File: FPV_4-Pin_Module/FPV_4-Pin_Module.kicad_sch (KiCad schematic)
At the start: 2 parts, among them J1 Conn_01x10_Socket, J2 Conn_01x10_Socket

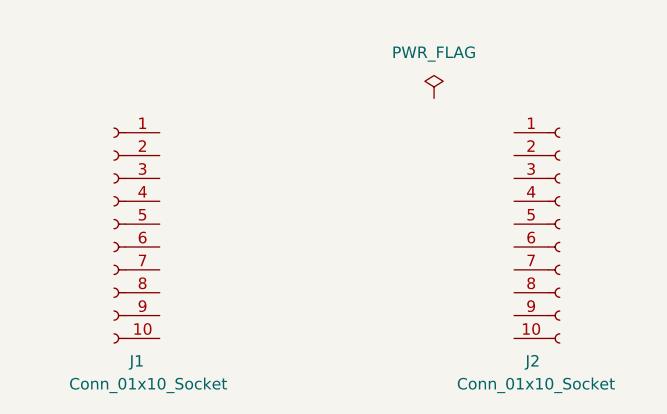
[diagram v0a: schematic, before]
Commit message: Adding FPV 4-pin interface module
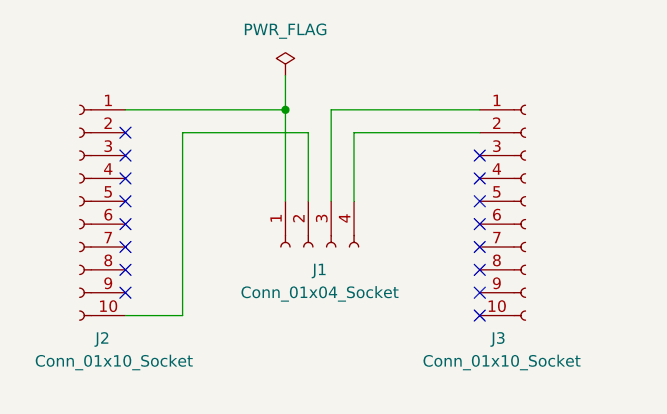
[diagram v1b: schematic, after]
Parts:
- removed J1: Conn_01x10_Socket, Connector_PinSocket_2.00mm:PinSocket_1x10_P2.00mm_Vertical, symbol Connector:Conn_01x10_Socket
- added J1: Conn_01x04_Socket, Connector_JST:JST_PH_B4B-PH-K_1x04_P2.00mm_Vertical, symbol Connector:Conn_01x04_Socket
- added J3: Conn_01x10_Socket, Connector_PinSocket_2.00mm:PinSocket_1x10_P2.00mm_Vertical, symbol Connector:Conn_01x10_Socket
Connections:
- net at J2.1 (Pin_1): now also J1.1 (Pin_1)
- net at J2.10 (Pin_10): now also J1.2 (Pin_2)
- new net: J1.3 (Pin_3), J3.1 (Pin_1)
- new net: J1.4 (Pin_4), J3.2 (Pin_2)
- no-connect marks 0 -> 16
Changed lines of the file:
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@@
 (kicad_sch (version 20230121) (generator eeschema)
   (paper "A4")
-  (symbol (lib_id "Connector:Conn_01x10_Socket") (at 121.92 95.25 0) (mirror y) (unit 1)
+  (junction (at 140.97 82.55) (diameter 0) (color 0 0 0 0)
+  )
+  (no_connect (at 123.19 100.33))
+  (no_connect (at 123.19 95.25))
+  (no_connect (at 162.56 100.33))
+  (no_connect (at 162.56 102.87))
+  (no_connect (at 123.19 90.17))
+  (no_connect (at 123.19 92.71))
+  (no_connect (at 162.56 97.79))
+  (no_connect (at 123.19 85.09))
+  (no_connect (at 162.56 87.63))
+  (no_connect (at 123.19 87.63))
+  (no_connect (at 162.56 105.41))
+  (no_connect (at 162.56 95.25))
+  (no_connect (at 123.19 102.87))
+  (no_connect (at 123.19 97.79))
+  (no_connect (at 162.56 92.71))
+  (no_connect (at 162.56 90.17))
+  (wire (pts (xy 129.54 105.41) (xy 123.19 105.41))
+    (stroke (width 0) (type default))
+  )
+  (wire (pts (xy 140.97 92.71) (xy 140.97 82.55))
+    (stroke (width 0) (type default))
+  )
+  (wire (pts (xy 146.05 82.55) (xy 162.56 82.55))
+    (stroke (width 0) (type default))
+  )
+  (wire (pts (xy 148.59 92.71) (xy 148.59 85.09))
+    (stroke (width 0) (type default))
+  )
+  (wire (pts (xy 143.51 92.71) (xy 143.51 85.09))
+    (stroke (width 0) (type default))
+  )
+  (wire (pts (xy 143.51 85.09) (xy 129.54 85.09))
+    (stroke (width 0) (type default))
+  )
+  (wire (pts (xy 146.05 92.71) (xy 146.05 82.55))
+    (stroke (width 0) (type default))
+  )
+  (wire (pts (xy 129.54 85.09) (xy 129.54 105.41))
+    (stroke (width 0) (type default))
+  )
+  (wire (pts (xy 140.97 78.74) (xy 140.97 82.55))
+    (stroke (width 0) (type default))
+  )
+  (wire (pts (xy 140.97 82.55) (xy 123.19 82.55))
+    (stroke (width 0) (type default))
+  )
+  (wire (pts (xy 148.59 85.09) (xy 162.56 85.09))
+    (stroke (width 0) (type default))
+  )
+  (symbol (lib_id "Connector:Conn_01x10_Socket") (at 167.64 92.71 0) (unit 1)
     (in_bom yes) (on_board yes) (dnp no)
-    (property "Reference" "J1" (at 124.46 110.49 0)
-      (effects (font (size 1.27 1.27)))
+    (property "Reference" "J3" (at 163.83 107.95 0)
+      (effects (font (size 1.27 1.27)) (justify left))
     )
-    (property "Value" "Conn_01x10_Socket" (at 125.73 113.03 0)
-      (effects (font (size 1.27 1.27)))
+    (property "Value" "Conn_01x10_Socket" (at 156.21 110.49 0)
+      (effects (font (size 1.27 1.27)) (justify left))
     )
-    (property "Footprint" "Connector_PinSocket_2.00mm:PinSocket_1x10_P2.00mm_Vertical" (at 121.92 95.25 0)
+    (property "Footprint" "Connector_PinSocket_2.00mm:PinSocket_1x10_P2.00mm_Vertical" (at 167.64 92.71 0)
       (effects (font (size 1.27 1.27)) hide)
     )
-    (property "Datasheet" "~" (at 121.92 95.25 0)
+    (property "Datasheet" "~" (at 167.64 92.71 0)
       (effects (font (size 1.27 1.27)) hide)
     )
@@
       (project "FPV_4-Pin_Module"
         (path "/7bf13dc3-6a85-4b7a-9483-4a4f8f99eecc"
-          (reference "J1") (unit 1)
+          (reference "J3") (unit 1)
         )
       )
       (project "USB_Module"
         (path "/d452682e-4b72-4fc8-ac9a-c22d1abda260"
-          (reference "J2") (unit 1)
+          (reference "J3") (unit 1)
         )
       )
       (project "FPV_3-Pin_Module"
         (path "/d88b4443-d914-4b47-8a50-2a5201342e50"
+          (reference "J3") (unit 1)
+        )
+      )
+    )
+  )
+  (symbol (lib_id "Connector:Conn_01x04_Socket") (at 143.51 97.79 90) (mirror x) (unit 1)
+    (in_bom yes) (on_board yes) (dnp no)
+    (property "Reference" "J1" (at 144.78 100.33 90)
+      (effects (font (size 1.27 1.27)))
+    )
+    (property "Value" "Conn_01x04_Socket" (at 144.78 102.87 90)
+      (effects (font (size 1.27 1.27)))
+    )
+    (property "Footprint" "Connector_JST:JST_PH_B4B-PH-K_1x04_P2.00mm_Vertical" (at 143.51 97.79 0)
+      (effects (font (size 1.27 1.27)) hide)
+    )
+    (property "Datasheet" "~" (at 143.51 97.79 0)
+      (effects (font (size 1.27 1.27)) hide)
+    )
+    (pin "1")
+    (pin "2")
+    (pin "3")
+    (pin "4")
+    (instances
+      (project "FPV_4-Pin_Module"
+        (path "/7bf13dc3-6a85-4b7a-9483-4a4f8f99eecc"
           (reference "J1") (unit 1)
         )
@@
     )
   )
-  (symbol (lib_id "power:PWR_FLAG") (at 157.48 81.28 0) (unit 1)
-    (in_bom yes) (on_board yes) (dnp no) (fields_autoplaced)
-    (property "Reference" "#FLG01" (at 157.48 79.375 0)
+  (symbol (lib_id "Connector:Conn_01x10_Socket") (at 118.11 92.71 0) (mirror y) (unit 1)
+    (in_bom yes) (on_board yes) (dnp no)
+    (property "Reference" "J2" (at 120.65 107.95 0)
+      (effects (font (size 1.27 1.27)))
+    )
+    (property "Value" "Conn_01x10_Socket" (at 121.92 110.49 0)
+      (effects (font (size 1.27 1.27)))
+    )
+    (property "Footprint" "Connector_PinSocket_2.00mm:PinSocket_1x10_P2.00mm_Vertical" (at 118.11 92.71 0)
       (effects (font (size 1.27 1.27)) hide)
     )
-    (property "Value" "PWR_FLAG" (at 157.48 76.2 0)
-      (effects (font (size 1.27 1.27)))
-    )
-    (property "Footprint" "" (at 157.48 81.28 0)
-      (effects (font (size 1.27 1.27)) hide)
-    )
-    (property "Datasheet" "~" (at 157.48 81.28 0)
-      (effects (font (size 1.27 1.27)) hide)
-    )
-    (pin "1")
-    (instances
-      (project "FPV_4-Pin_Module"
-        (path "/7bf13dc3-6a85-4b7a-9483-4a4f8f99eecc"
-          (reference "#FLG01") (unit 1)
-        )
-      )
-      (project "USB_Module"
-        (path "/d452682e-4b72-4fc8-ac9a-c22d1abda260"
-          (reference "#FLG02") (unit 1)
-        )
-      )
-      (project "FPV_3-Pin_Module"
-        (path "/d88b4443-d914-4b47-8a50-2a5201342e50"
-          (reference "#FLG02") (unit 1)
-        )
-      )
-    )
-  )
-  (symbol (lib_id "Connector:Conn_01x10_Socket") (at 171.45 95.25 0) (unit 1)
-    (in_bom yes) (on_board yes) (dnp no)
-    (property "Reference" "J2" (at 167.64 110.49 0)
-      (effects (font (size 1.27 1.27)) (justify left))
-    )
-    (property "Value" "Conn_01x10_Socket" (at 160.02 113.03 0)
-      (effects (font (size 1.27 1.27)) (justify left))
-    )
-    (property "Footprint" "Connector_PinSocket_2.00mm:PinSocket_1x10_P2.00mm_Vertical" (at 171.45 95.25 0)
-      (effects (font (size 1.27 1.27)) hide)
-    )
-    (property "Datasheet" "~" (at 171.45 95.25 0)
+    (property "Datasheet" "~" (at 118.11 92.71 0)
       (effects (font (size 1.27 1.27)) hide)
     )
@@
       (project "USB_Module"
         (path "/d452682e-4b72-4fc8-ac9a-c22d1abda260"
-          (reference "J3") (unit 1)
+          (reference "J2") (unit 1)
         )
       )
       (project "FPV_3-Pin_Module"
         (path "/d88b4443-d914-4b47-8a50-2a5201342e50"
-          (reference "J3") (unit 1)
+          (reference "J1") (unit 1)
         )
       )
+    )
+  )
+  (symbol (lib_id "power:PWR_FLAG") (at 140.97 78.74 0) (unit 1)
+    (in_bom yes) (on_board yes) (dnp no) (fields_autoplaced)
+    (property "Reference" "#FLG01" (at 140.97 76.835 0)
+      (effects (font (size 1.27 1.27)) hide)
+    )
+    (property "Value" "PWR_FLAG" (at 140.97 73.66 0)
+      (effects (font (size 1.27 1.27)))
+    )
+    (property "Footprint" "" (at 140.97 78.74 0)
+      (effects (font (size 1.27 1.27)) hide)
+    )
+    (property "Datasheet" "~" (at 140.97 78.74 0)
+      (effects (font (size 1.27 1.27)) hide)
+    )
+    (pin "1")
+    (instances
+      (project "FPV_4-Pin_Module"
+        (path "/7bf13dc3-6a85-4b7a-9483-4a4f8f99eecc"
+          (reference "#FLG01") (unit 1)
+        )
+      )
+      (project "USB_Module"
+        (path "/d452682e-4b72-4fc8-ac9a-c22d1abda260"
+          (reference "#FLG02") (unit 1)
+        )
+      )
+      (project "FPV_3-Pin_Module"
+        (path "/d88b4443-d914-4b47-8a50-2a5201342e50"
+          (reference "#FLG02") (unit 1)
+        )
+      )
